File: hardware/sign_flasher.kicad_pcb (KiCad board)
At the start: 2 copper layers, 99.1 x 99.1 mm, 50 parts, among them J1 Power, Q1 BC557, Q2 BC547, U1 NE555D, U2 NE555D

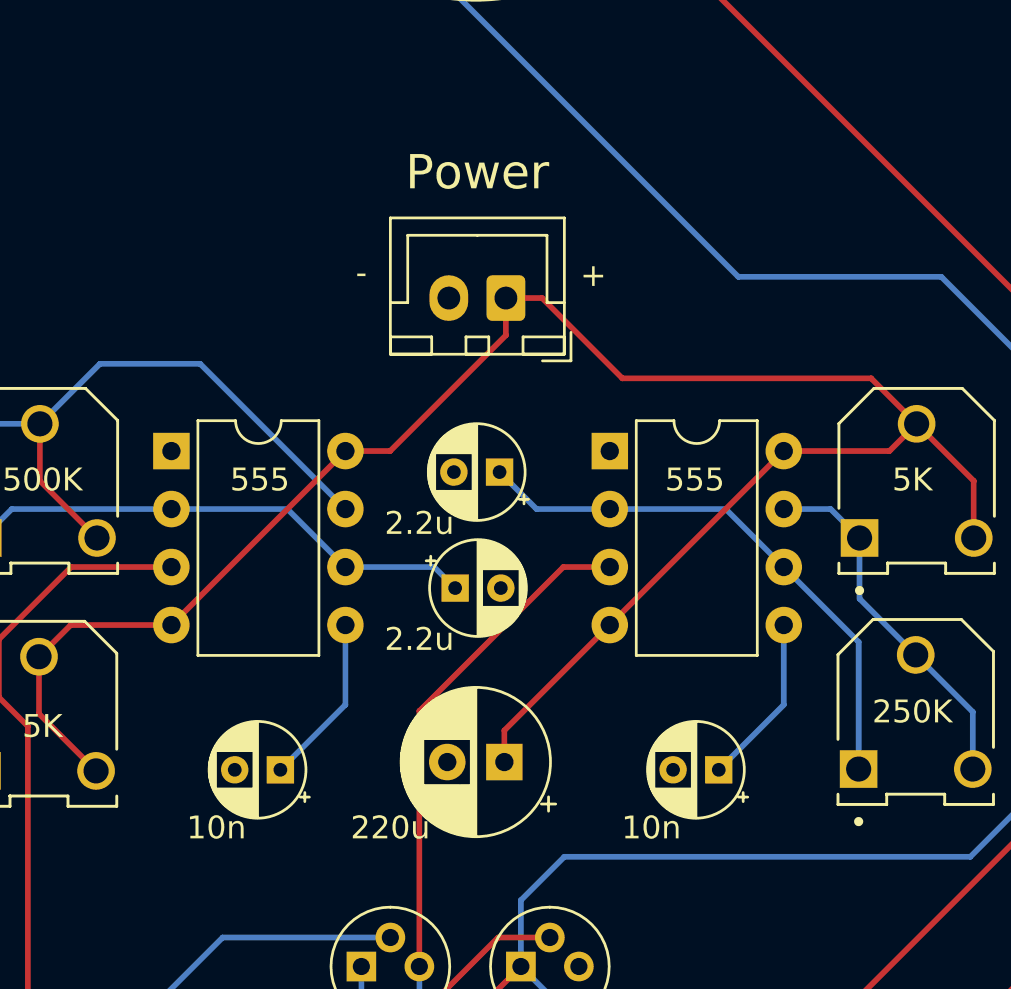
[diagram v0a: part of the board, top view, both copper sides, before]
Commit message: Address issues identified with rev v0.01:
 - Revise schematic to indicate the need for 12V power
 - Add reverse voltage protection diode
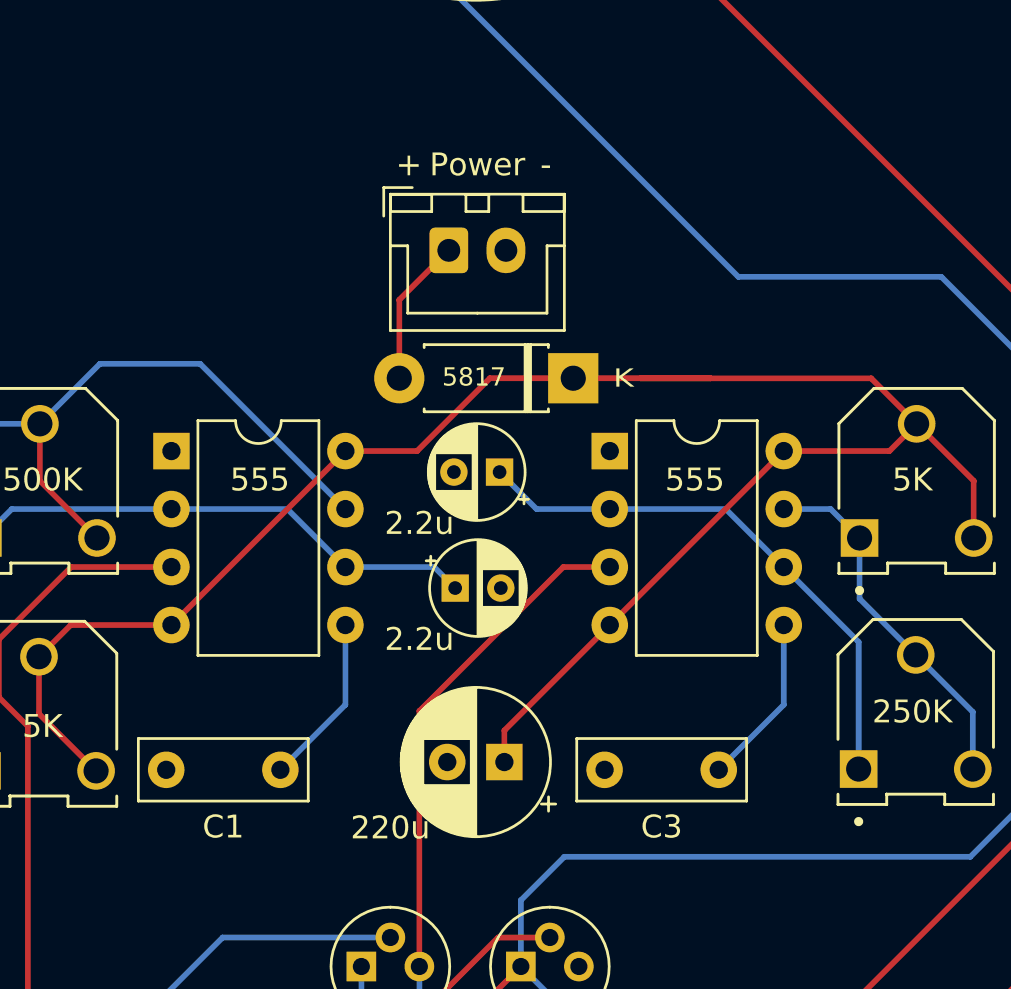
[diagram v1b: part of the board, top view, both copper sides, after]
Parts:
- added D25: 5817, Diode_THT:D_DO-41_SOD81_P7.62mm_Horizontal, F.Cu at (137.6, 90.8)
- C1, C3: footprint Capacitor_THT:CP_Radial_D4.0mm_P2.00mm -> Capacitor_THT:C_Rect_L7.2mm_W2.5mm_P5.00mm_FKS2_FKP2_MKS2_MKP2
- moved J1 3.26 mm to (132.1, 85.2), turned to 0 degrees
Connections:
- C5 pad 1: /9V0 -> /12V0
- J1 pad 1: /9V0 -> /VPOS
- RV1 pad 2: /9V0 -> /12V0
- RV1 pad 3: /9V0 -> /12V0
- RV3 pad 2: /9V0 -> /12V0
- RV3 pad 3: /9V0 -> /12V0
- U1 pad 4: /9V0 -> /12V0
- U1 pad 8: /9V0 -> /12V0
- U2 pad 4: /9V0 -> /12V0
- U2 pad 8: /9V0 -> /12V0
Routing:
- net /9V0: track 85.3 -> 0.00 mm
- net /12V0: track 0.00 -> 84.4 mm
- net /VPOS: track 0.00 -> 6.50 mm

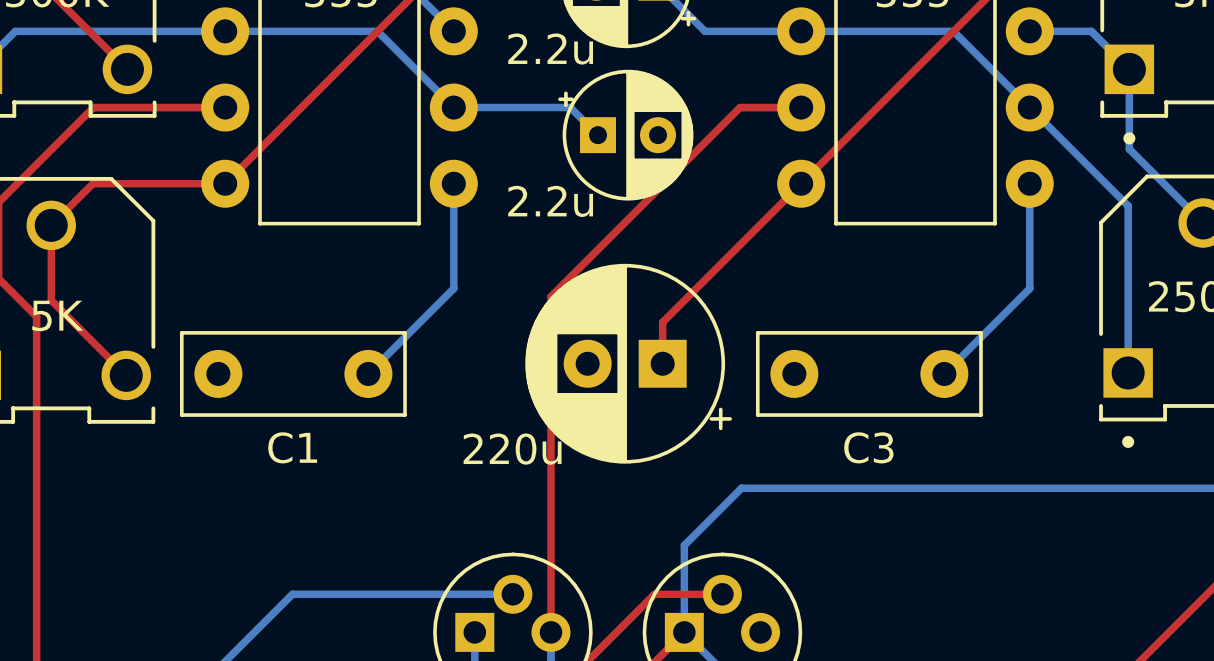
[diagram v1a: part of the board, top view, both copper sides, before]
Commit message: adjust position of replaced capacitor footprint
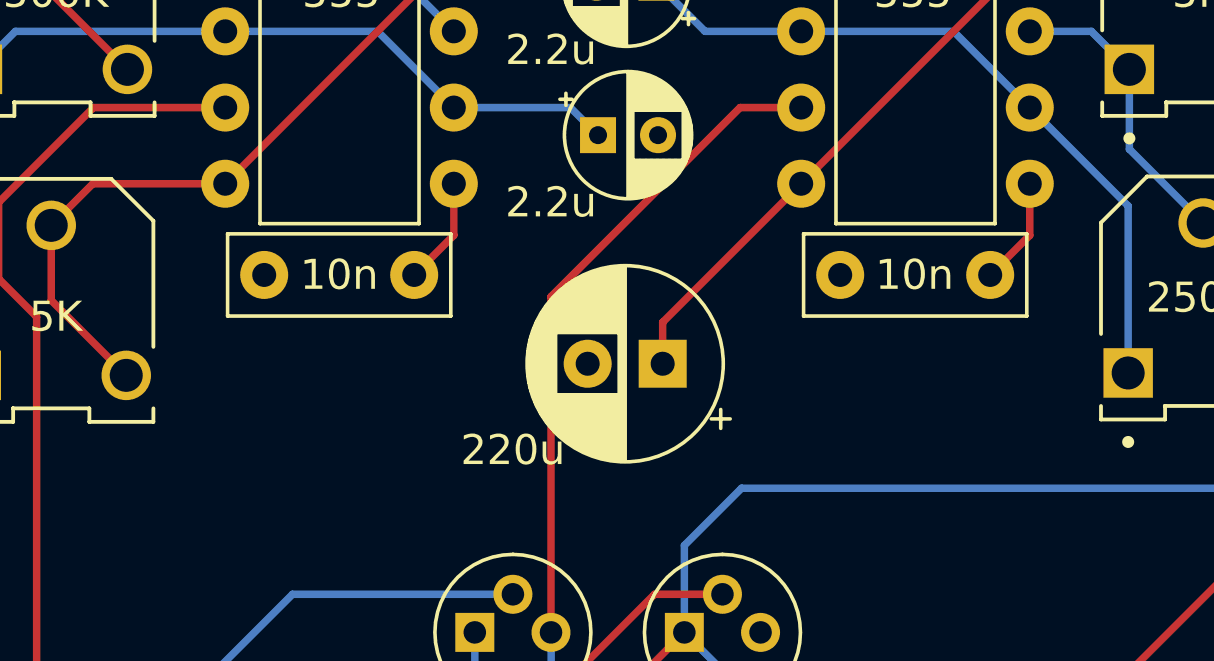
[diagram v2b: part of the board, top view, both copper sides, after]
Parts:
- moved C3 3.64 mm to (145.4, 104.7)
- moved C1 3.64 mm to (126.2, 104.7)
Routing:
- net Net-(U2-CV): track 7.52 -> 3.59 mm
- net Net-(U1-CV): track 7.52 -> 3.59 mm
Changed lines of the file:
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@@
   )
   (footprint "Capacitor_THT:C_Rect_L7.2mm_W2.5mm_P5.00mm_FKS2_FKP2_MKS2_MKP2" (layer "F.Cu")
-    (at 124.72325 107.95 180)
+    (at 126.25 104.65 180)
     (descr "C, Rect series, Radial, pin pitch=5.00mm, , length*width=7.2*2.5mm^2, Capacitor, http://www.wima.com/EN/WIMA_FKS_2.pdf")
     (tags "C Rect series Radial pin pitch 5.00mm  length 7.2mm width 2.5mm Capacitor")
@@
     (property "ki_keywords" "cap capacitor")
     (attr through_hole)
-    (fp_text reference "C1" (at 2.5 -2.5 180) (layer "F.SilkS")
-        (effects (font (size 1 1) (thickness 0.15)))
-    )
-    (fp_text value "10n" (at 2.5 2.5 180) (layer "F.Fab")
+    (fp_text reference "C1" (at 2.5 -2.5 180) (layer "F.Fab")
+        (effects (font (size 1 1) (thickness 0.15)))
+    )
+    (fp_text value "10n" (at 2.5 0 180) (layer "F.SilkS")
         (effects (font (size 1 1) (thickness 0.15)))
     )
@@
   )
   (footprint "Capacitor_THT:C_Rect_L7.2mm_W2.5mm_P5.00mm_FKS2_FKP2_MKS2_MKP2" (layer "F.Cu")
-    (at 143.92195 107.95 180)
+    (at 145.44935 104.65 180)
     (descr "C, Rect series, Radial, pin pitch=5.00mm, , length*width=7.2*2.5mm^2, Capacitor, http://www.wima.com/EN/WIMA_FKS_2.pdf")
     (tags "C Rect series Radial pin pitch 5.00mm  length 7.2mm width 2.5mm Capacitor")
@@
     (property "ki_keywords" "cap capacitor")
     (attr through_hole)
-    (fp_text reference "C3" (at 2.5 -2.5 180) (layer "F.SilkS")
-        (effects (font (size 1 1) (thickness 0.15)))
-    )
-    (fp_text value "10n" (at 2.5 2.5 180) (layer "F.Fab")
+    (fp_text reference "C3" (at 2.5 -2.5 180) (layer "F.Fab")
+        (effects (font (size 1 1) (thickness 0.15)))
+    )
+    (fp_text value "10n" (at 2.52195 0 180) (layer "F.SilkS")
         (effects (font (size 1 1) (thickness 0.15)))
     )
@@
   (segment (start 134.53238 106.22697) (end 139.14935 101.61) (width 0.25) (layer "F.Cu") (net 1))
   (segment (start 146.76935 93.99) (end 139.14935 101.61) (width 0.25) (layer "F.Cu") (net 1))
-  (segment (start 127.57065 101.61) (end 127.57065 105.1026) (width 0.25) (layer "B.Cu") (net 3))
-  (segment (start 127.57065 105.1026) (end 124.72325 107.95) (width 0.25) (layer "B.Cu") (net 3))
-  (segment (start 146.76935 101.61) (end 146.76935 105.1026) (width 0.25) (layer "B.Cu") (net 4))
-  (segment (start 146.76935 105.1026) (end 143.92195 107.95) (width 0.25) (layer "B.Cu") (net 4))
+  (segment (start 127.57065 103.32935) (end 126.25 104.65) (width 0.25) (layer "F.Cu") (net 3))
+  (segment (start 127.57065 101.61) (end 127.57065 103.32935) (width 0.25) (layer "F.Cu") (net 3))
+  (segment (start 146.76935 103.33) (end 145.44935 104.65) (width 0.25) (layer "F.Cu") (net 4))
+  (segment (start 146.76935 101.61) (end 146.76935 103.33) (width 0.25) (layer "F.Cu") (net 4))
   (segment (start 131.457401 99.07) (end 132.377401 99.99) (width 0.25) (layer "B.Cu") (net 5))
   (segment (start 112.9588 96.53) (end 111.6913 97.7975) (width 0.25) (layer "B.Cu") (net 5))
